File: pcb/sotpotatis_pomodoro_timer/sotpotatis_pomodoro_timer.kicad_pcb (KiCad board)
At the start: 4 copper layers, 81.1 x 58.7 mm, 57 parts, among them J2 USB_C_PWR_IN, SW1 LEFT_BTN, SW2 PRESET_1_BTN, SW3 PRESET_2_BTN, SW4 PRESET_3_BTN, SW5 RIGHT_BTN, SW6 PWR_SWITCH, U1 ATtiny84A-P

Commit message: add: Backup spaghetti Charlieplexing wiring :)
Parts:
- removed G*** (x9): LOGO, LOGO
- removed REF** (x4): MountingHole_3.2mm_M3, MountingHole:MountingHole_3.2mm_M3
- added H1: MountingHole, MountingHole:MountingHole_3.2mm_M3, F.Cu at (96.3, 47.8)
- added H2: MountingHole, MountingHole:MountingHole_3.2mm_M3, F.Cu at (167.8, 47.8)
- added H3: MountingHole, MountingHole:MountingHole_3.2mm_M3, F.Cu at (96.3, 96.8)
- added H4: MountingHole, MountingHole:MountingHole_3.2mm_M3, F.Cu at (167.8, 96.8)
- R2, R5: moved to F.Cu
- moved D14 2.54 mm to (169.1, 59.8), turned to 180 degrees
- turned R2 to 180 degrees
- turned R3 to 180 degrees
- turned R4 to 180 degrees
- turned R5 to 180 degrees
- renumbered G*** to LB1, G*** to LB2
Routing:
- net (no net): track 381.5 -> 0.00 mm
- net Net-(D11-A): track 0.00 -> 93.6 mm, vias 0 -> 1
- net Net-(D10-A): track 0.00 -> 92.3 mm, vias 0 -> 1
- net Net-(D1-K): track 0.00 -> 91.1 mm, vias 0 -> 2
- net Net-(D1-A): track 0.00 -> 65.6 mm, vias 0 -> 1
- net Net-(D13-K): track 0.00 -> 38.8 mm
- net PB0: track 0.00 -> 2.65 mm
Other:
- board text removed: "1.25mm bold"
- board text removed: "1.25mm not bold"
- board text removed: "1.5mm bold"
- board text removed: "1.5mm not bold"
- board text removed: "12mm width"
- board text removed: "16mm width"
- board text removed: "1mm bold"
- board text removed: "1mm not bold"
- board text removed: "2.5mm bold"
- board text removed: "2.5mm not bold"
- board text removed: "24mm width"
- board text removed: "2mm bold"
- board text removed: "2mm not bold"
- board text removed: "3mm bold"
- board text removed: "3mm not bold"
- board text removed: "SIZE TEST"

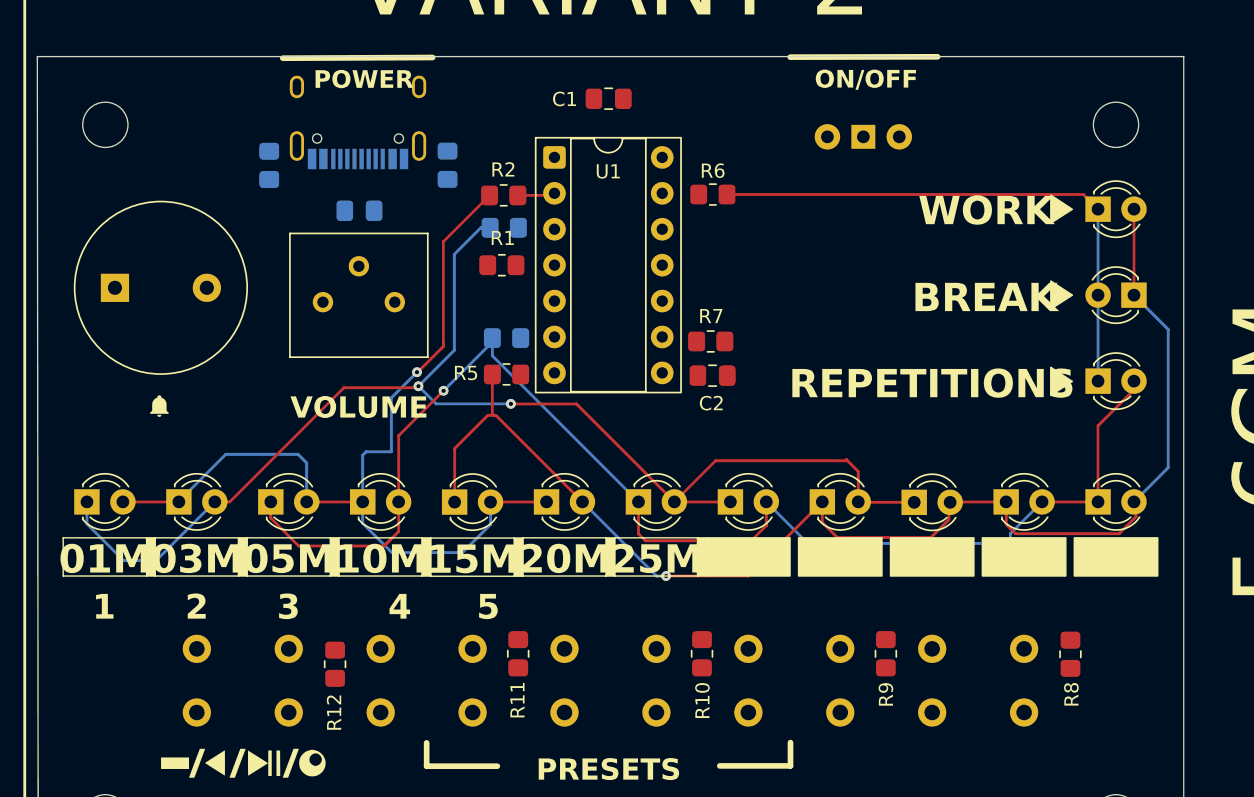
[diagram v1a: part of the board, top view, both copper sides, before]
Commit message: add: Backup PCB routing progress before board reversal...
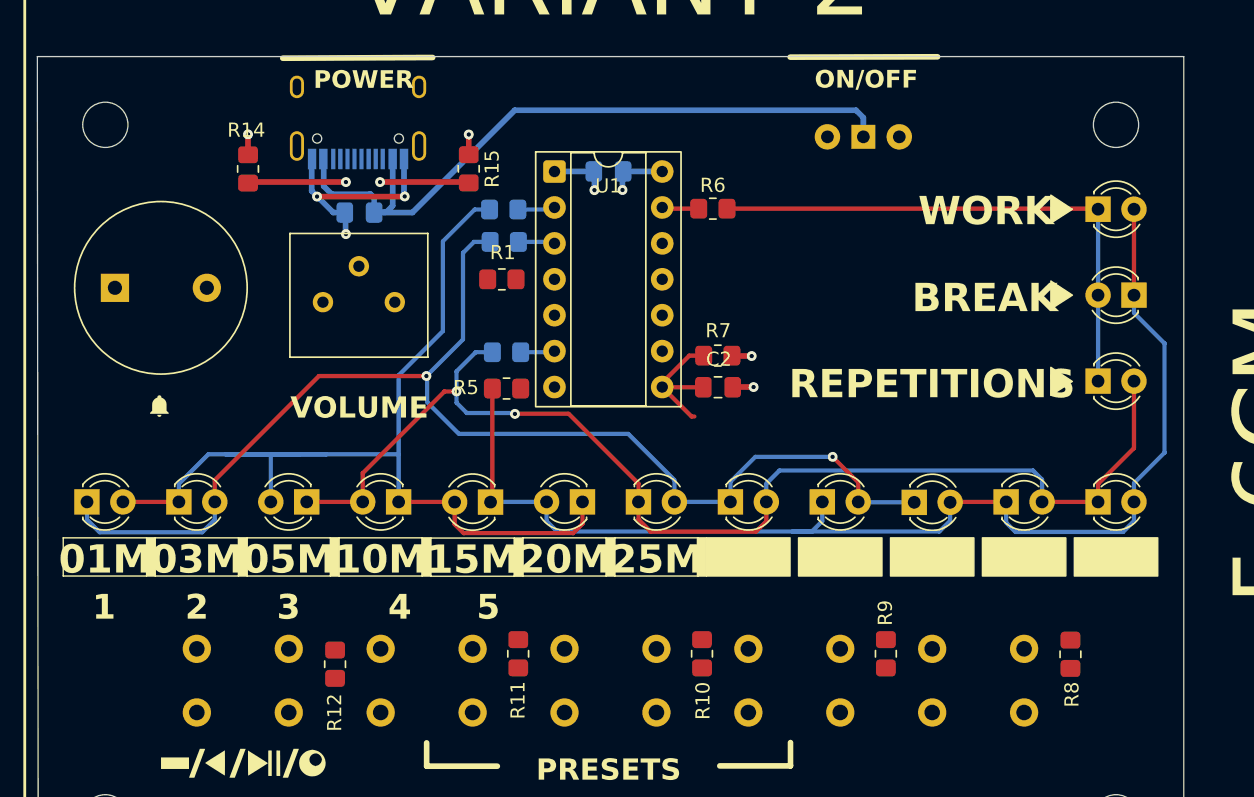
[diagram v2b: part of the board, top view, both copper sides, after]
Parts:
- C1, R2: moved to B.Cu
- R14, R15: moved to F.Cu
- moved C1 5.15 mm to (131.9, 51.1)
- moved D3 2.54 mm to (110.6, 74.4), turned to 180 degrees
- moved D4 2.54 mm to (117.1, 74.4), turned to 180 degrees
- moved D5 2.54 mm to (123.6, 74.5), turned to 180 degrees
- moved D6 2.54 mm to (130.1, 74.4), turned to 180 degrees
- moved R14 1.52 mm to (106.4, 50.9)
- moved R15 1.52 mm to (122.0, 50.9)
- moved R7 1.12 mm to (139.6, 64.1)
- moved R1 1.00 mm to (124.4, 58.7)
- moved R2 1.00 mm to (124.5, 53.8)
- moved R3 1.00 mm to (124.5, 56.1)
- moved R4 1.00 mm to (124.7, 63.9)
- moved R5 1.00 mm to (124.7, 66.4)
- moved R6 1.00 mm to (139.3, 53.7)
- moved U1 1.00 mm to (128.1, 51.1)
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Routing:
- net +5V: track 0.00 -> 50.8 mm
- net GND: track 0.00 -> 24.0 mm, vias 0 -> 7
- net PA5: track 0.00 -> 9.78 mm
- net Net-(D1-A): track 65.6 -> 74.7 mm, vias 1 -> 0
- net Net-(D11-A): track 93.6 -> 85.6 mm, vias 1 -> 2
- net Net-(J2-CC1): track 0.00 -> 6.95 mm, vias 0 -> 1
- net Net-(J2-CC2): track 0.00 -> 6.55 mm, vias 0 -> 1
- net VCC: track 0.00 -> 5.69 mm, vias 0 -> 2
- net Net-(D10-A): track 92.3 -> 87.3 mm, vias 1 -> 0
- net Net-(D1-K): track 91.1 -> 88.3 mm
- net PA0: track 0.00 -> 2.62 mm
- net PB1: track 0.00 -> 2.59 mm
- net PA7: track 0.00 -> 2.42 mm
- added copper zone on In1.Cu, net GND
- added copper zone on In2.Cu, net VCC
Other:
- board text added: "1MM"

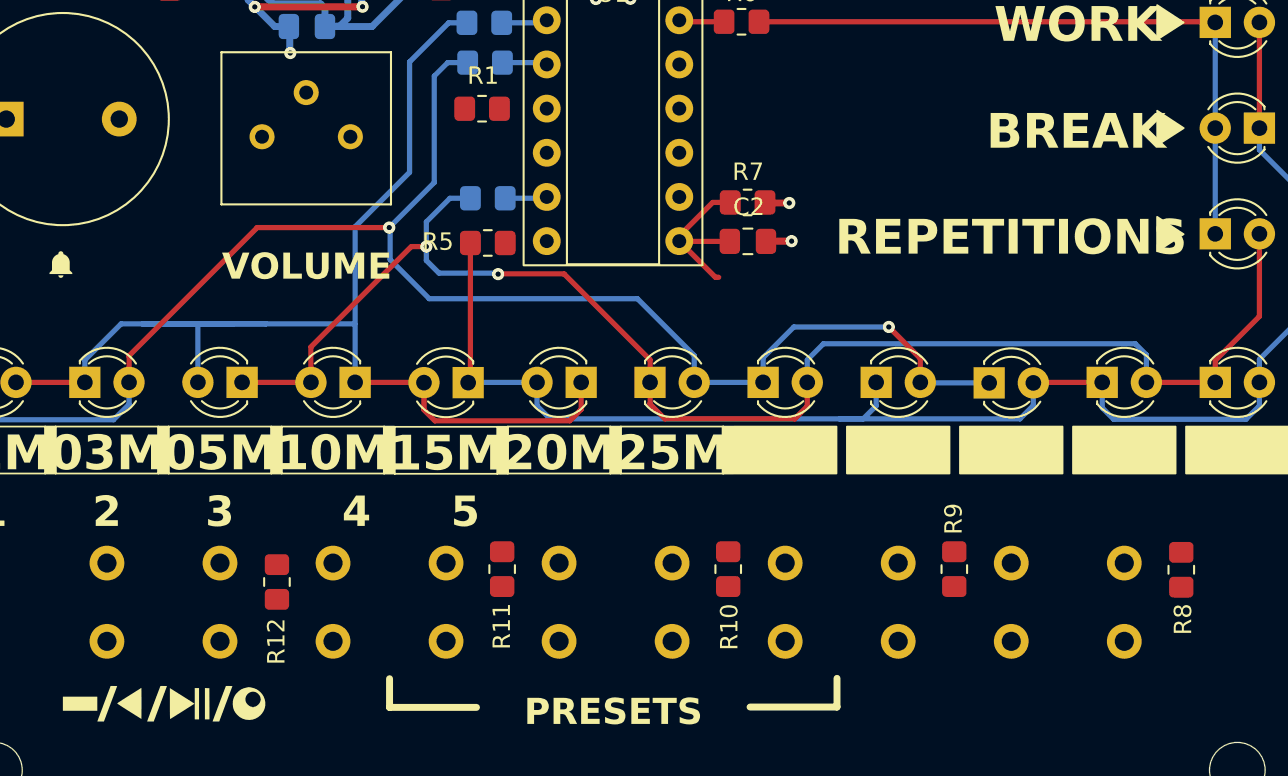
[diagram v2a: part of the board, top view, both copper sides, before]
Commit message: add: Route everything but buzzer (No reversal needed)
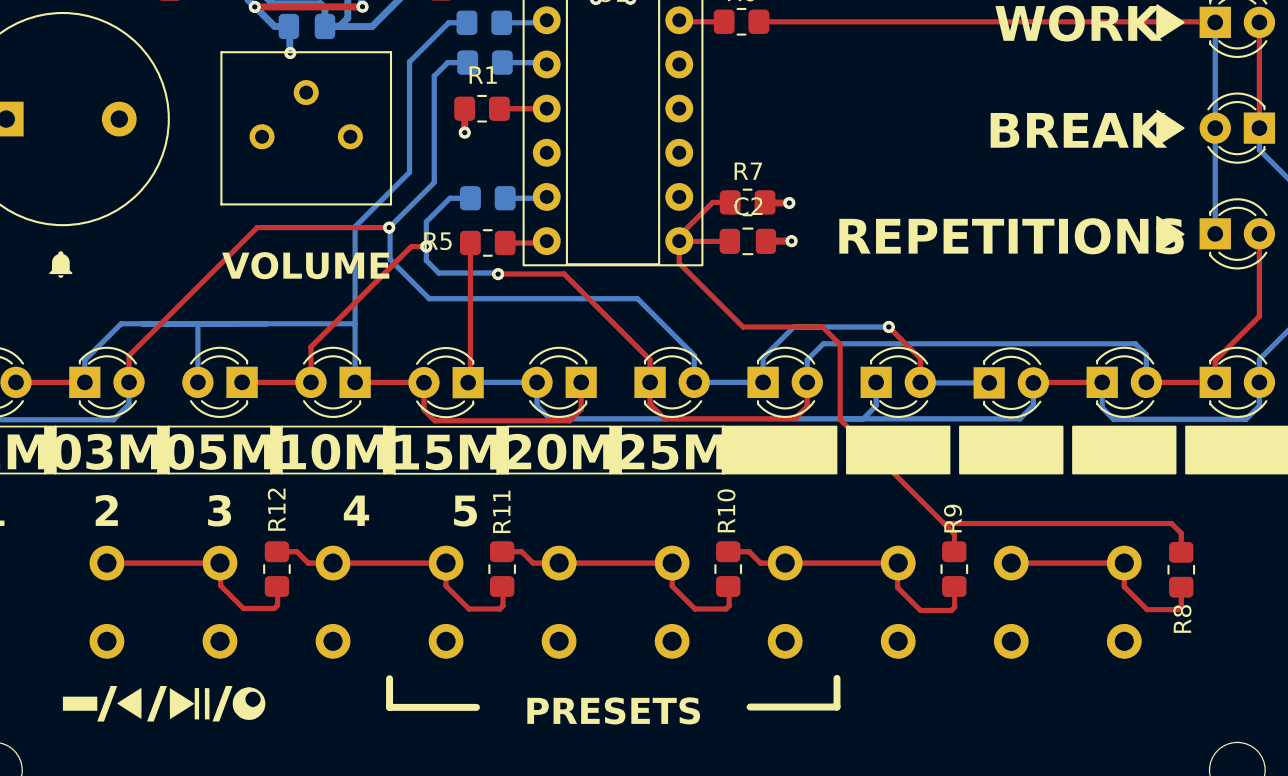
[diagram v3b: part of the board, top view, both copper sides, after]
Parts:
- moved R12 0.74 mm to (112.6, 85.2), turned to -90 degrees
- turned R10 to -90 degrees
- turned R11 to -90 degrees
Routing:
- net PA5: track 9.78 -> 48.7 mm
- net Net-(R11-Pad2): track 0.00 -> 16.4 mm
- net Net-(R10-Pad2): track 0.00 -> 16.4 mm
- net Net-(R10-Pad1): track 0.00 -> 16.4 mm
- net Net-(R8-Pad1): track 0.00 -> 13.5 mm
- net Net-(R12-Pad2): track 0.00 -> 12.9 mm
- net Net-(U1-~{RESET}/PB3): track 0.00 -> 2.72 mm
- net PA6: track 0.00 -> 2.43 mm
- net VCC: track 5.69 -> 7.11 mm, vias 2 -> 3

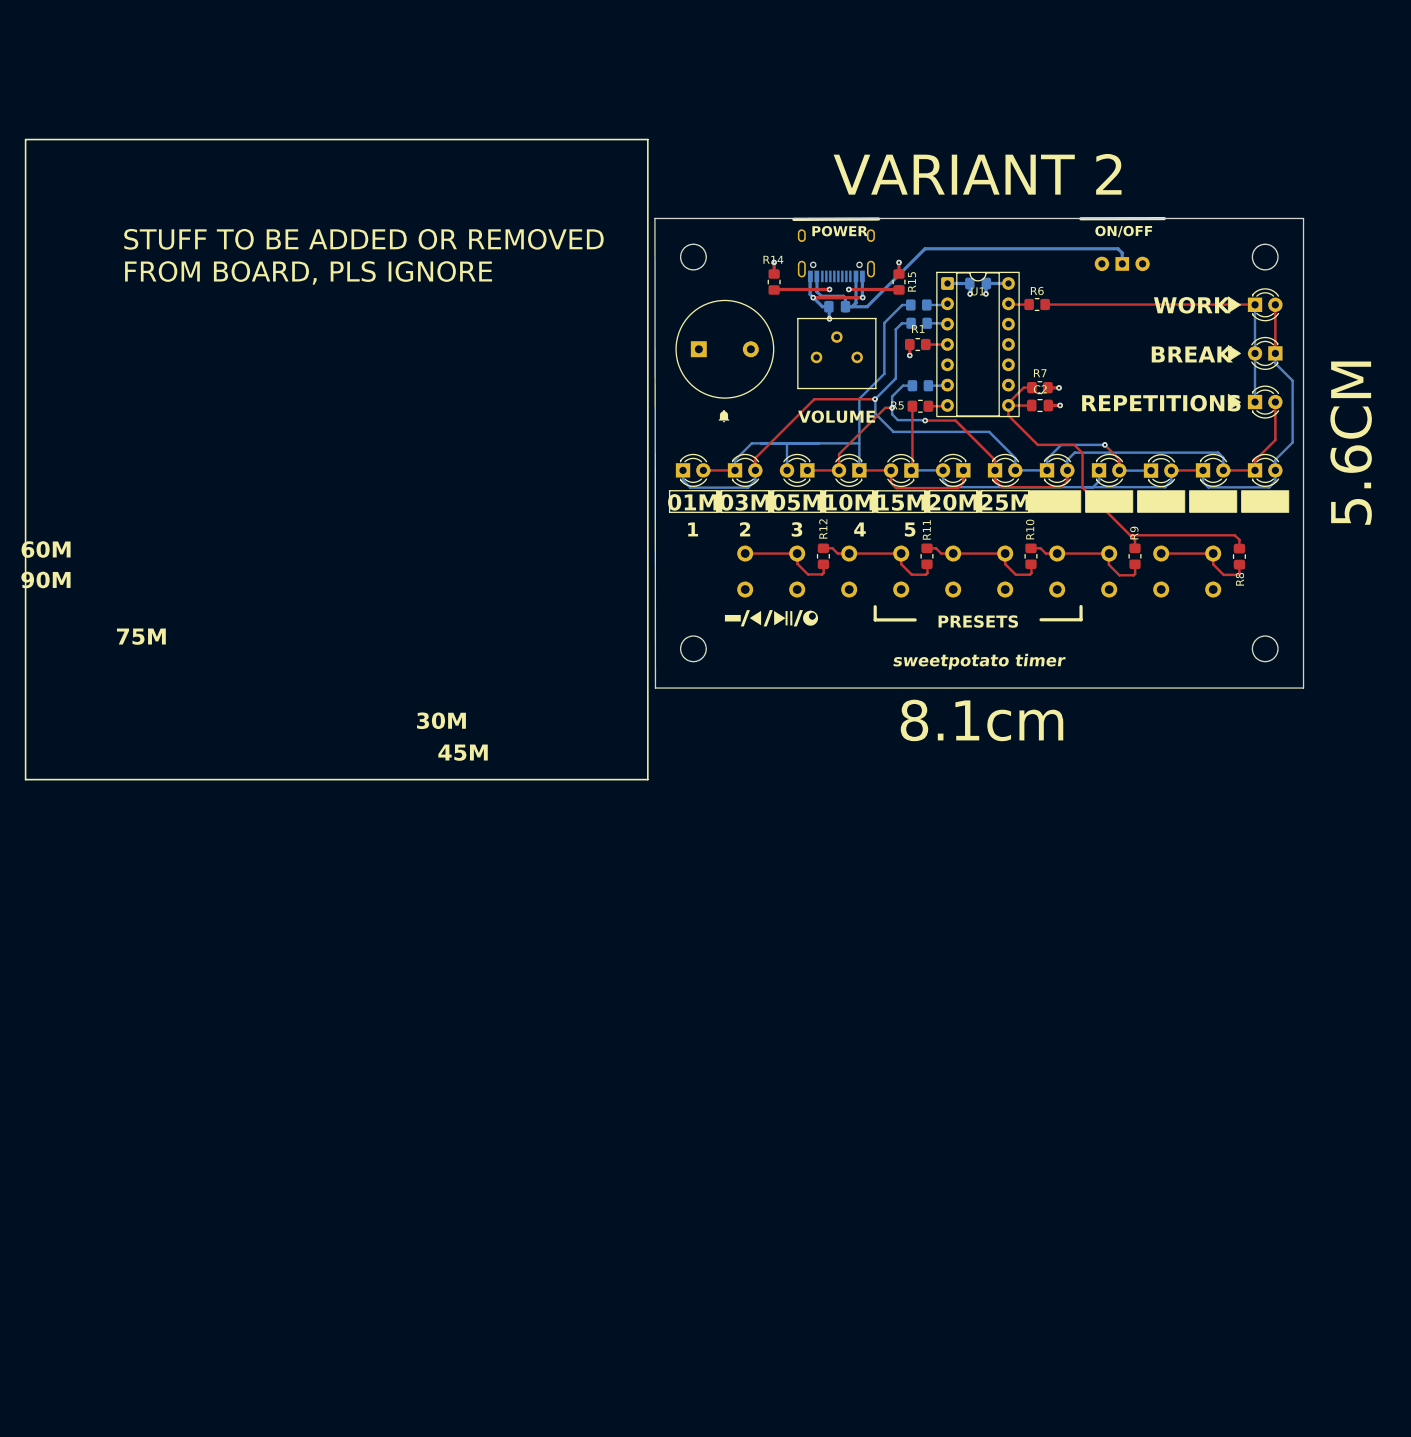
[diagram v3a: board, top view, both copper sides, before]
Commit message: fix: Finish silkscreen time scale for LEDs
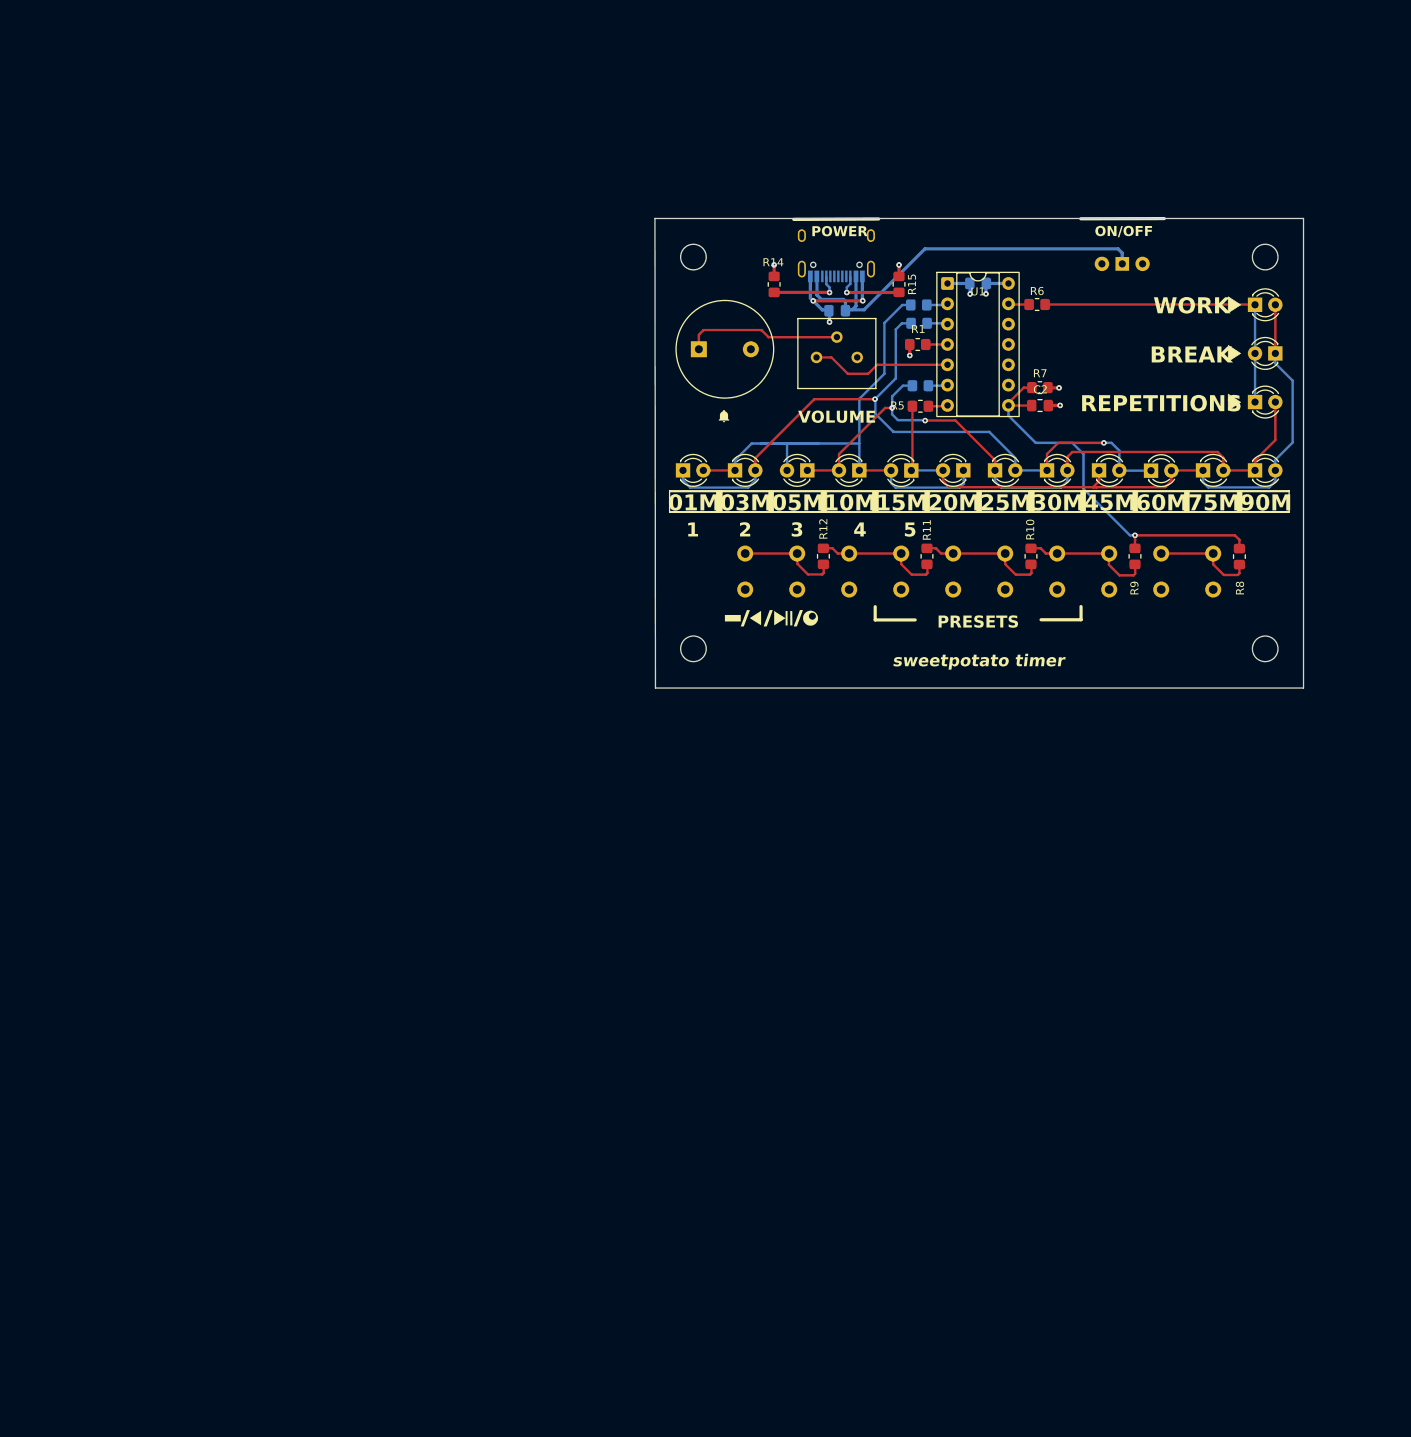
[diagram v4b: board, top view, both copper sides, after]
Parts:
- moved C3 0.50 mm to (114.3, 54.5)
- moved R14 0.30 mm to (106.4, 51.2)
- moved R15 0.30 mm to (122.0, 51.2)
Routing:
- net Net-(BZ1-+): track 0.00 -> 19.7 mm
- net PB2: track 0.00 -> 17.7 mm
- net Net-(J2-CC2): track 6.55 -> 9.01 mm
- net Net-(J2-CC1): track 6.95 -> 9.20 mm
- net Net-(D1-K): track 88.3 -> 89.5 mm
- net GND: track 24.0 -> 25.0 mm
- net Net-(D10-A): track 87.3 -> 86.4 mm
- net PA5: track 48.7 -> 48.5 mm, vias 0 -> 1
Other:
- board text removed: "5.6CM"
- board text removed: "8.1cm"
- board text removed: "Board center"
- board text removed: "PUT ICONS HERE AND NEWLINES?"
- board text removed: "STUFF TO BE ADDED OR REMOVED FROM BOARD, PLS IGNORE"
- board text removed: "VARIANT 2"
